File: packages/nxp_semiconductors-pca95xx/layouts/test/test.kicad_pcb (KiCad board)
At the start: 2 copper layers, 14 parts

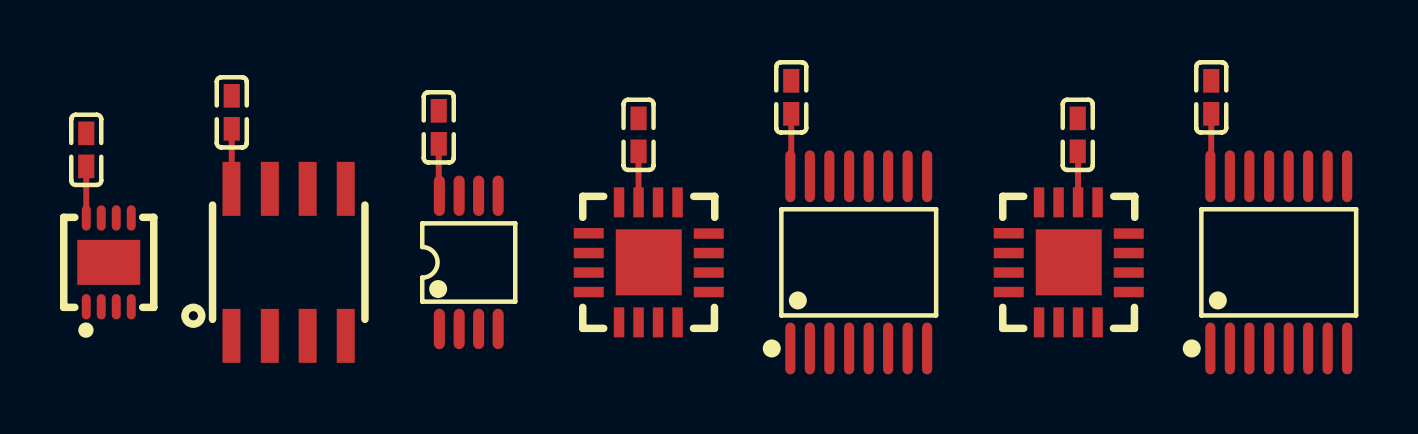
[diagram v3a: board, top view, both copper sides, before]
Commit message: Update 3D model locations
fix missing renders
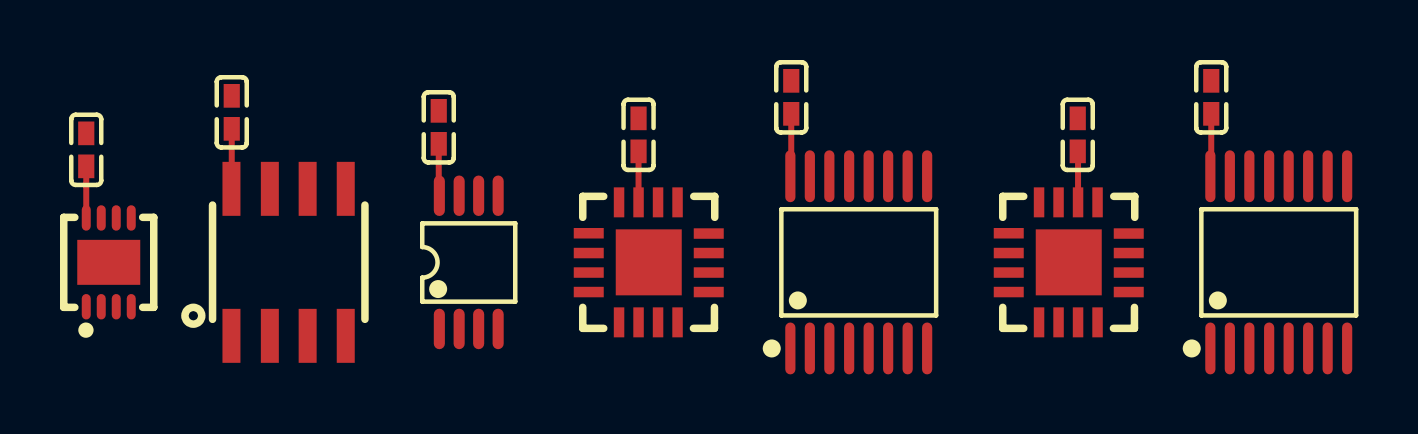
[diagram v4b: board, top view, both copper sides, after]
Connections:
- U1 pad 1: io[0]-2 -> io[0]-3
- U1 pad 2: io[1]-3 -> io[1]-6
- U1 pad 3: io[2]-6 -> io[2]-4
- U1 pad 5: io[3]-2 -> io[3]-3
- U2 pad 1: io[0] -> io[0]-6
- U2 pad 2: io[1]-5 -> io[1]-4
- U2 pad 3: io[2]-3 -> io[2]-6
- U2 pad 5: io[3]-6 -> io[3]-4
- U3 pad 1: io[0]-6 -> io[0]
- U3 pad 2: io[1] -> io[1]-5
- U3 pad 3: io[2] -> io[2]-3
- U3 pad 5: io[3] -> io[3]-5
- U4 pad 10: io[7]-2 -> io[7]
- U4 pad 2: io[0]-5 -> io[0]-4
- U4 pad 3: io[1]-6 -> io[1]-3
- U4 pad 4: io[2]-2 -> io[2]-5
- U4 pad 5: io[3]-5 -> io[3]-6
- U4 pad 7: io[4]-2 -> io[4]
- U4 pad 8: io[5]-3 -> io[5]-1
- U5 pad 11: io[6]-2 -> io[6]-1
- U5 pad 12: io[7] -> io[7]-2
- U5 pad 13: interrupt-2 -> interrupt-3
- U5 pad 4: io[0]-1 -> io[0]-5
- U5 pad 5: io[1]-4 -> io[1]-1
- U5 pad 6: io[2]-5 -> io[2]-1
- U5 pad 7: io[3]-1 -> io[3]-2
- U5 pad 9: io[4]-3 -> io[4]-1
- U6 pad 11: interrupt-3 -> interrupt-1
- U6 pad 2: io[0]-3 -> io[0]-2
- U6 pad 3: io[1]-1 -> io[1]-2
- U6 pad 4: io[2]-4 -> io[2]
- U6 pad 5: io[3]-4 -> io[3]-1
- U6 pad 7: io[4] -> io[4]-3
- U6 pad 8: io[5]-1 -> io[5]-3
- U6 pad 9: io[6] -> io[6]-2
- U7 pad 11: io[6]-1 -> io[6]
- U7 pad 13: interrupt-1 -> interrupt-2
- U7 pad 4: io[0]-4 -> io[0]-1
- U7 pad 5: io[1]-2 -> io[1]
- U7 pad 6: io[2]-1 -> io[2]-2
- U7 pad 7: io[3]-3 -> io[3]
- U7 pad 9: io[4]-1 -> io[4]-2

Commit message: rebuild all packages & regenerate images of changed layouts (silk)
Add new scripts for version bump and build (based on atopile/packages)
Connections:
- U1 pad 1: io[0]-3 -> io[0]-6
- U1 pad 3: io[2]-4 -> io[2]-6
- U1 pad 5: io[3]-3 -> io[3]-6
- U2 pad 1: io[0]-6 -> io[0]-1
- U2 pad 2: io[1]-4 -> io[1]-1
- U2 pad 3: io[2]-6 -> io[2]-1
- U2 pad 5: io[3]-4 -> io[3]-1
- U3 pad 2: io[1]-5 -> io[1]
- U3 pad 3: io[2]-3 -> io[2]
- U3 pad 5: io[3]-5 -> io[3]
- U4 pad 10: io[7] -> io[7]-1
- U4 pad 11: interrupt -> interrupt-1
- U4 pad 2: io[0]-4 -> io[0]-3
- U4 pad 4: io[2]-5 -> io[2]-3
- U4 pad 5: io[3]-6 -> io[3]-3
- U4 pad 7: io[4] -> io[4]-1
- U4 pad 9: io[6]-3 -> io[6]-1
- U5 pad 10: io[5]-2 -> io[5]-3
- U5 pad 11: io[6]-1 -> io[6]-3
- U5 pad 12: io[7]-2 -> io[7]-3
- U5 pad 5: io[1]-1 -> io[1]-5
- U5 pad 6: io[2]-1 -> io[2]-5
- U5 pad 7: io[3]-2 -> io[3]-5
- U5 pad 9: io[4]-1 -> io[4]-3
- U6 pad 10: io[7]-3 -> io[7]
- U6 pad 11: interrupt-1 -> interrupt
- U6 pad 4: io[2] -> io[2]-2
- U6 pad 5: io[3]-1 -> io[3]-2
- U6 pad 7: io[4]-3 -> io[4]
- U6 pad 8: io[5]-3 -> io[5]
- U6 pad 9: io[6]-2 -> io[6]
- U7 pad 10: io[5] -> io[5]-2
- U7 pad 11: io[6] -> io[6]-2
- U7 pad 12: io[7]-1 -> io[7]-2
- U7 pad 4: io[0]-1 -> io[0]-4
- U7 pad 5: io[1] -> io[1]-4
- U7 pad 6: io[2]-2 -> io[2]-4
- U7 pad 7: io[3] -> io[3]-4
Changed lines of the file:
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@@
     (net 0 "")
     (net 1 "gnd")
-    (net 2 "io[1]-5")
-    (net 3 "io[3]-5")
-    (net 4 "io[4]-1")
-    (net 5 "io[1]-1")
-    (net 6 "io[4]")
-    (net 7 "io[5]-2")
-    (net 8 "io[0]-1")
-    (net 9 "io[7]")
-    (net 10 "io[3]-2")
-    (net 11 "io[7]-1")
-    (net 12 "io[3]")
-    (net 13 "io[2]-4")
-    (net 14 "io[6]-1")
-    (net 15 "io[3]-4")
-    (net 16 "io[6]")
+    (net 2 "io[1]")
+    (net 3 "io[3]")
+    (net 4 "io[4]-3")
+    (net 5 "io[1]-5")
+    (net 6 "io[4]-1")
+    (net 7 "io[5]-3")
+    (net 8 "io[0]-4")
+    (net 9 "io[7]-1")
+    (net 10 "io[3]-5")
+    (net 11 "io[7]-2")
+    (net 12 "io[3]-4")
+    (net 13 "io[2]-6")
+    (net 14 "io[6]-3")
+    (net 15 "io[3]-1")
+    (net 16 "io[6]-2")
     (net 17 "scl")
     (net 18 "io[1]-2")
-    (net 19 "io[5]")
-    (net 20 "io[3]-3")
+    (net 19 "io[5]-2")
+    (net 20 "io[3]-6")
     (net 21 "io[1]-3")
-    (net 22 "io[6]-2")
+    (net 22 "io[6]")
     (net 23 "io[4]-2")
-    (net 24 "io[0]-3")
-    (net 25 "io[3]-6")
-    (net 26 "io[2]-2")
-    (net 27 "io[7]-2")
-    (net 28 "io[5]-3")
-    (net 29 "io[0]-4")
+    (net 24 "io[0]-6")
+    (net 25 "io[3]-3")
+    (net 26 "io[2]-4")
+    (net 27 "io[7]-3")
+    (net 28 "io[5]")
+    (net 29 "io[0]-3")
     (net 30 "io[0]-5")
-    (net 31 "io[2]")
-    (net 32 "io[2]-1")
-    (net 33 "io[1]-4")
-    (net 34 "io[3]-1")
-    (net 35 "io[6]-3")
-    (net 36 "io[1]")
+    (net 31 "io[2]-2")
+    (net 32 "io[2]-5")
+    (net 33 "io[1]-1")
+    (net 34 "io[3]-2")
+    (net 35 "io[6]-1")
+    (net 36 "io[1]-4")
     (net 37 "interrupt-3")
     (net 38 "interrupt-2")
-    (net 39 "io[4]-3")
-    (net 40 "io[2]-6")
+    (net 39 "io[4]")
+    (net 40 "io[2]-1")
     (net 41 "sda")
-    (net 42 "io[7]-3")
-    (net 43 "io[0]-6")
+    (net 42 "io[7]")
+    (net 43 "io[0]-1")
     (net 44 "io[1]-6")
-    (net 45 "interrupt")
+    (net 45 "interrupt-1")
     (net 46 "io[5]-1")
-    (net 47 "io[2]-5")
+    (net 47 "io[2]-3")
     (net 48 "io[0]")
     (net 49 "io[0]-2")
-    (net 50 "io[2]-3")
-    (net 51 "interrupt-1")
+    (net 50 "io[2]")
+    (net 51 "interrupt")
     (net 52 "vdd")
     (footprint "NXP_Semicon_PCA9554APW_118:TSSOP-16_L5.0-W4.4-P0.65-LS6.4-BL"
@@
             (size 0.34 1.73)
             (layers "F.Cu" "F.Mask" "F.Paste")
-            (net 8 "io[0]-1")
+            (net 8 "io[0]-4")
         )
         (pad "5" smd oval
@@
             (size 0.34 1.73)
             (layers "F.Cu" "F.Mask" "F.Paste")
-            (net 36 "io[1]")
+            (net 36 "io[1]-4")
         )
         (pad "6" smd oval
@@
             (size 0.34 1.73)
             (layers "F.Cu" "F.Mask" "F.Paste")
-            (net 26 "io[2]-2")
+            (net 26 "io[2]-4")
         )
         (pad "7" smd oval
@@
             (size 0.34 1.73)
             (layers "F.Cu" "F.Mask" "F.Paste")
-            (net 12 "io[3]")
+            (net 12 "io[3]-4")
         )
         (pad "8" smd oval
@@
             (size 0.34 1.73)
             (layers "F.Cu" "F.Mask" "F.Paste")
-            (net 19 "io[5]")
+            (net 19 "io[5]-2")
         )
         (pad "11" smd oval
@@
             (size 0.34 1.73)
             (layers "F.Cu" "F.Mask" "F.Paste")
-            (net 16 "io[6]")
+            (net 16 "io[6]-2")
         )
         (pad "12" smd oval
@@
             (size 0.34 1.73)
             (layers "F.Cu" "F.Mask" "F.Paste")
-            (net 11 "io[7]-1")
+            (net 11 "io[7]-2")
         )
         (pad "13" smd oval
@@
             (size 0.3 0.85)
             (layers "F.Cu" "F.Mask" "F.Paste")
-            (net 24 "io[0]-3")
+            (net 24 "io[0]-6")
         )
         (pad "2" smd oval
@@
             (size 0.3 0.85)
             (layers "F.Cu" "F.Mask" "F.Paste")
-            (net 13 "io[2]-4")
+            (net 13 "io[2]-6")
         )
         (pad "4" smd oval
@@
             (size 0.3 0.85)
             (layers "F.Cu" "F.Mask" "F.Paste")
-            (net 20 "io[3]-3")
+            (net 20 "io[3]-6")
         )
         (pad "6" smd oval
@@
             (size 0.37 1.35)
             (layers "F.Cu" "F.Mask" "F.Paste")
-            (net 2 "io[1]-5")
+            (net 2 "io[1]")
         )
         (pad "3" smd oval
@@
             (size 0.37 1.35)
             (layers "F.Cu" "F.Mask" "F.Paste")
-            (net 50 "io[2]-3")
+            (net 50 "io[2]")
         )
         (pad "4" smd oval
@@
             (size 0.37 1.35)
             (layers "F.Cu" "F.Mask" "F.Paste")
-            (net 3 "io[3]-5")
+            (net 3 "io[3]")
         )
         (pad "6" smd oval
@@
             (size 0.35 1)
             (layers "F.Cu" "F.Mask" "F.Paste")
-            (net 31 "io[2]")
+            (net 31 "io[2]-2")
         )
         (pad "5" smd rect
@@
             (size 0.35 1)
             (layers "F.Cu" "F.Mask" "F.Paste")
-            (net 34 "io[3]-1")
+            (net 34 "io[3]-2")
         )
         (pad "6" smd rect
@@
             (size 0.35 1)
             (layers "F.Cu" "F.Mask" "F.Paste")
-            (net 39 "io[4]-3")
+            (net 39 "io[4]")
         )
         (pad "8" smd rect
@@
             (size 0.35 1)
             (layers "F.Cu" "F.Mask" "F.Paste")
-            (net 28 "io[5]-3")
+            (net 28 "io[5]")
         )
         (pad "9" smd rect
@@
             (size 0.35 1)
             (layers "F.Cu" "F.Mask" "F.Paste")
-            (net 22 "io[6]-2")
+            (net 22 "io[6]")
         )
         (pad "10" smd rect
@@
             (size 0.35 1)
             (layers "F.Cu" "F.Mask" "F.Paste")
-            (net 42 "io[7]-3")
+            (net 42 "io[7]")
         )
         (pad "11" smd rect
@@
             (size 0.35 1)
             (layers "F.Cu" "F.Mask" "F.Paste")
-            (net 51 "interrupt-1")
+            (net 51 "interrupt")
         )
         (pad "12" smd rect
@@
             (size 0.6 1.8)
             (layers "F.Cu" "F.Mask" "F.Paste")
-            (net 43 "io[0]-6")
+            (net 43 "io[0]-1")
         )
         (pad "2" smd rect
@@
             (size 0.6 1.8)
             (layers "F.Cu" "F.Mask" "F.Paste")
-            (net 33 "io[1]-4")
+            (net 33 "io[1]-1")
         )
         (pad "3" smd rect
@@
             (size 0.6 1.8)
             (layers "F.Cu" "F.Mask" "F.Paste")
-            (net 40 "io[2]-6")
+            (net 40 "io[2]-1")
         )
         (pad "4" smd rect
@@
             (size 0.6 1.8)
             (layers "F.Cu" "F.Mask" "F.Paste")
-            (net 15 "io[3]-4")
+            (net 15 "io[3]-1")
         )
         (pad "6" smd rect
@@
             (size 0.34 1.73)
             (layers "F.Cu" "F.Mask" "F.Paste")
-            (net 5 "io[1]-1")
+            (net 5 "io[1]-5")
         )
         (pad "6" smd oval
@@
             (size 0.34 1.73)
             (layers "F.Cu" "F.Mask" "F.Paste")
-            (net 32 "io[2]-1")
+            (net 32 "io[2]-5")
         )
         (pad "7" smd oval
@@
             (size 0.34 1.73)
             (layers "F.Cu" "F.Mask" "F.Paste")
-            (net 10 "io[3]-2")
+            (net 10 "io[3]-5")
         )
         (pad "8" smd oval
@@
             (size 0.34 1.73)
             (layers "F.Cu" "F.Mask" "F.Paste")
-            (net 4 "io[4]-1")
+            (net 4 "io[4]-3")
         )
         (pad "10" smd oval
@@
             (size 0.34 1.73)
             (layers "F.Cu" "F.Mask" "F.Paste")
-            (net 7 "io[5]-2")
+            (net 7 "io[5]-3")
         )
         (pad "11" smd oval
@@
             (size 0.34 1.73)
             (layers "F.Cu" "F.Mask" "F.Paste")
-            (net 14 "io[6]-1")
+            (net 14 "io[6]-3")
         )
         (pad "12" smd oval
@@
             (size 0.34 1.73)
             (layers "F.Cu" "F.Mask" "F.Paste")
-            (net 27 "io[7]-2")
+            (net 27 "io[7]-3")
         )
         (pad "13" smd oval
@@
             (size 0.35 1)
             (layers "F.Cu" "F.Mask" "F.Paste")
-            (net 29 "io[0]-4")
+            (net 29 "io[0]-3")
         )
         (pad "3" smd rect
@@
             (size 0.35 1)
             (layers "F.Cu" "F.Mask" "F.Paste")
-            (net 47 "io[2]-5")
+            (net 47 "io[2]-3")
         )
         (pad "5" smd rect
@@
             (size 0.35 1)
             (layers "F.Cu" "F.Mask" "F.Paste")
-            (net 25 "io[3]-6")
+            (net 25 "io[3]-3")
         )
         (pad "6" smd rect
@@
             (size 0.35 1)
             (layers "F.Cu" "F.Mask" "F.Paste")
-            (net 6 "io[4]")
+            (net 6 "io[4]-1")
         )
         (pad "8" smd rect
@@
             (size 0.35 1)
             (layers "F.Cu" "F.Mask" "F.Paste")
-            (net 35 "io[6]-3")
+            (net 35 "io[6]-1")
         )
         (pad "10" smd rect
@@
             (size 0.35 1)
             (layers "F.Cu" "F.Mask" "F.Paste")
-            (net 9 "io[7]")
+            (net 9 "io[7]-1")
         )
         (pad "11" smd rect
@@
             (size 0.35 1)
             (layers "F.Cu" "F.Mask" "F.Paste")
-            (net 45 "interrupt")
+            (net 45 "interrupt-1")
         )
         (pad "12" smd rect
